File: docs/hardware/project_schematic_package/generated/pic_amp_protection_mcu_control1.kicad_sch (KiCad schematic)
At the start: 9 parts, among them J3 LCD_I2C, Q1 Q_NMOS, U1 PIC16F18855-xSO

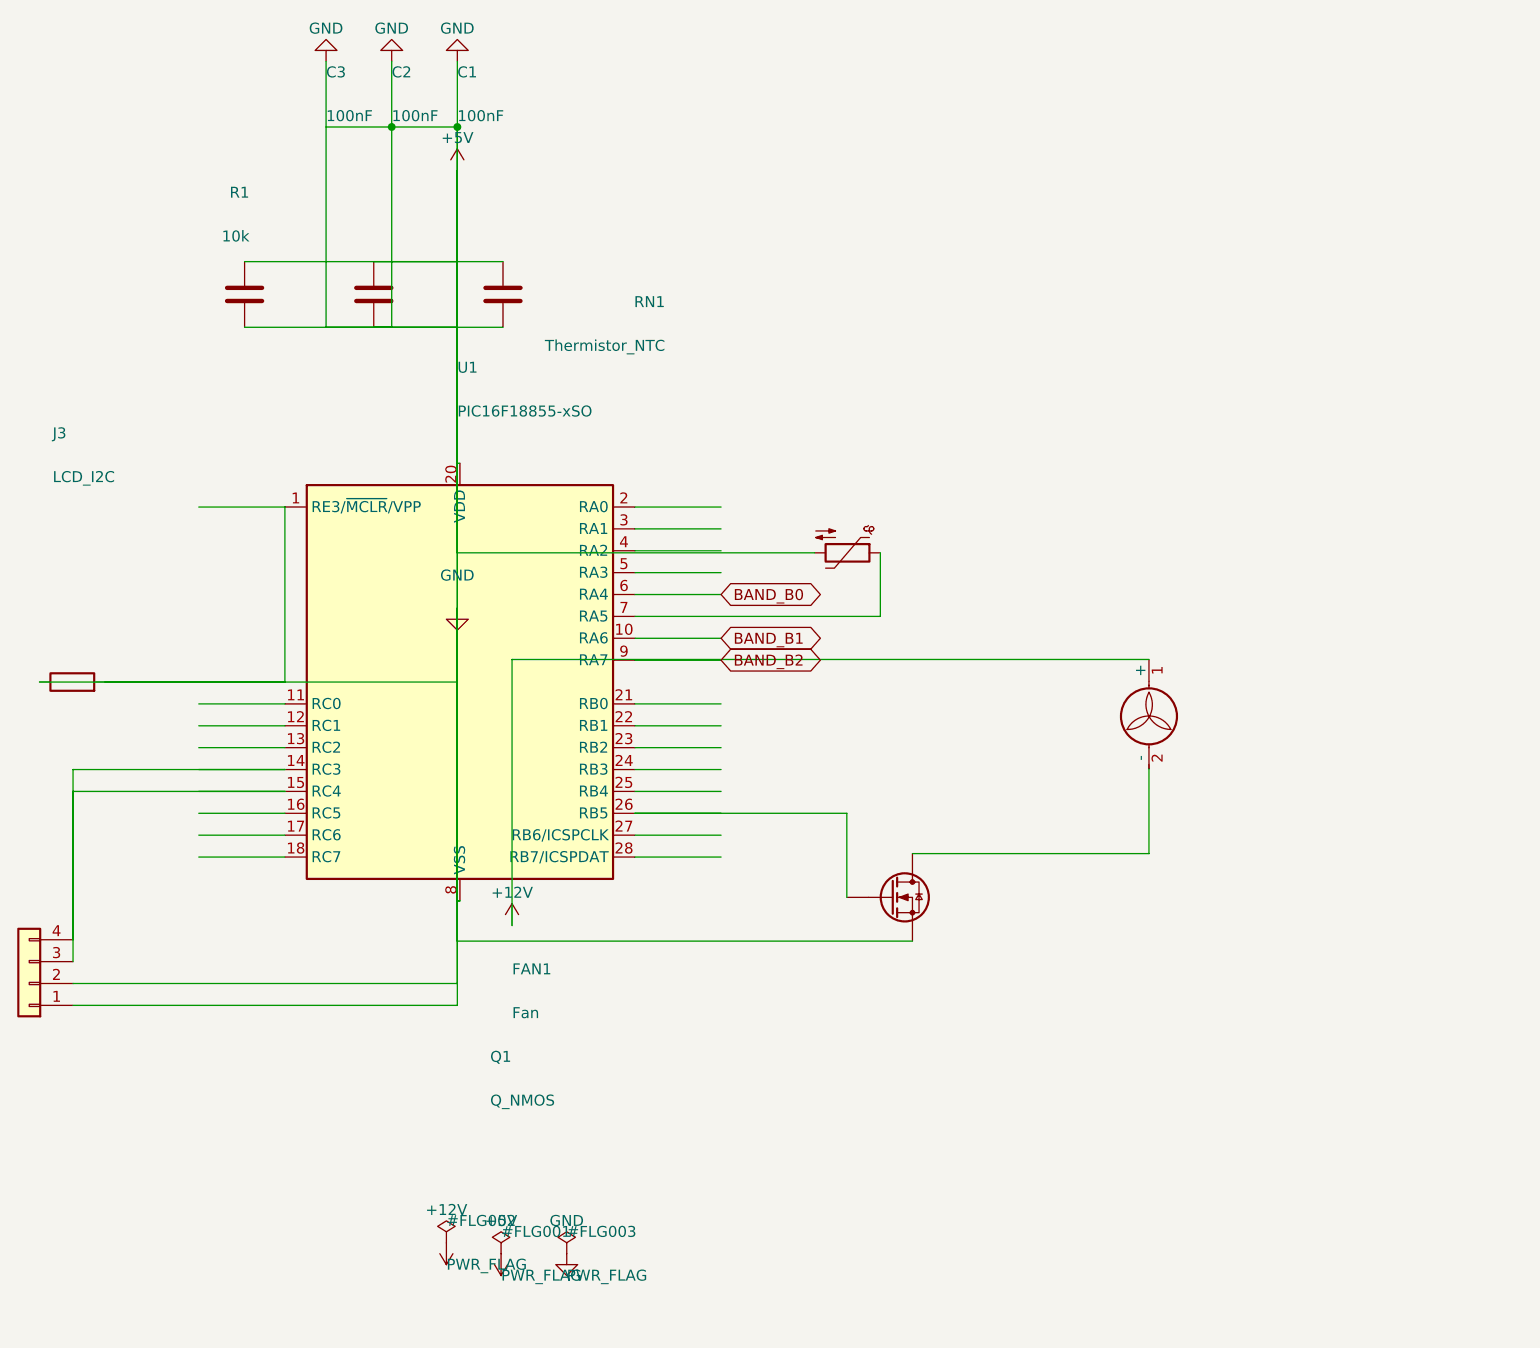
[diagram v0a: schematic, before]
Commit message: Add external interface connectors to complete MCU wiring
- J4 PTT_COMP_IF: PTT, comparator reset, overcurrent fault, GND
- J5 ENCODER: encoder A/B/switch, GND
- J6 TX_SEQ_TRIP: TX, TX_VCC, TX_BIAS, trip status, GND
- J7 SWR_SENSE: SWR1/SWR2 forward/reflected, GND
- J8 ANALOG_SENSE: current, overdrive, drain sense, GND

Wires every previously-unconnected U1 pin to one of these headers.
ERC unconnected-pin count: 17 -> 0. Remaining ERC output is limited to
pre-existing lib_symbol_mismatch/endpoint_off_grid warnings and the
standard PWR_FLAG-on-GND power_output/power_output pairing, consistent
with patterns already present in this file.
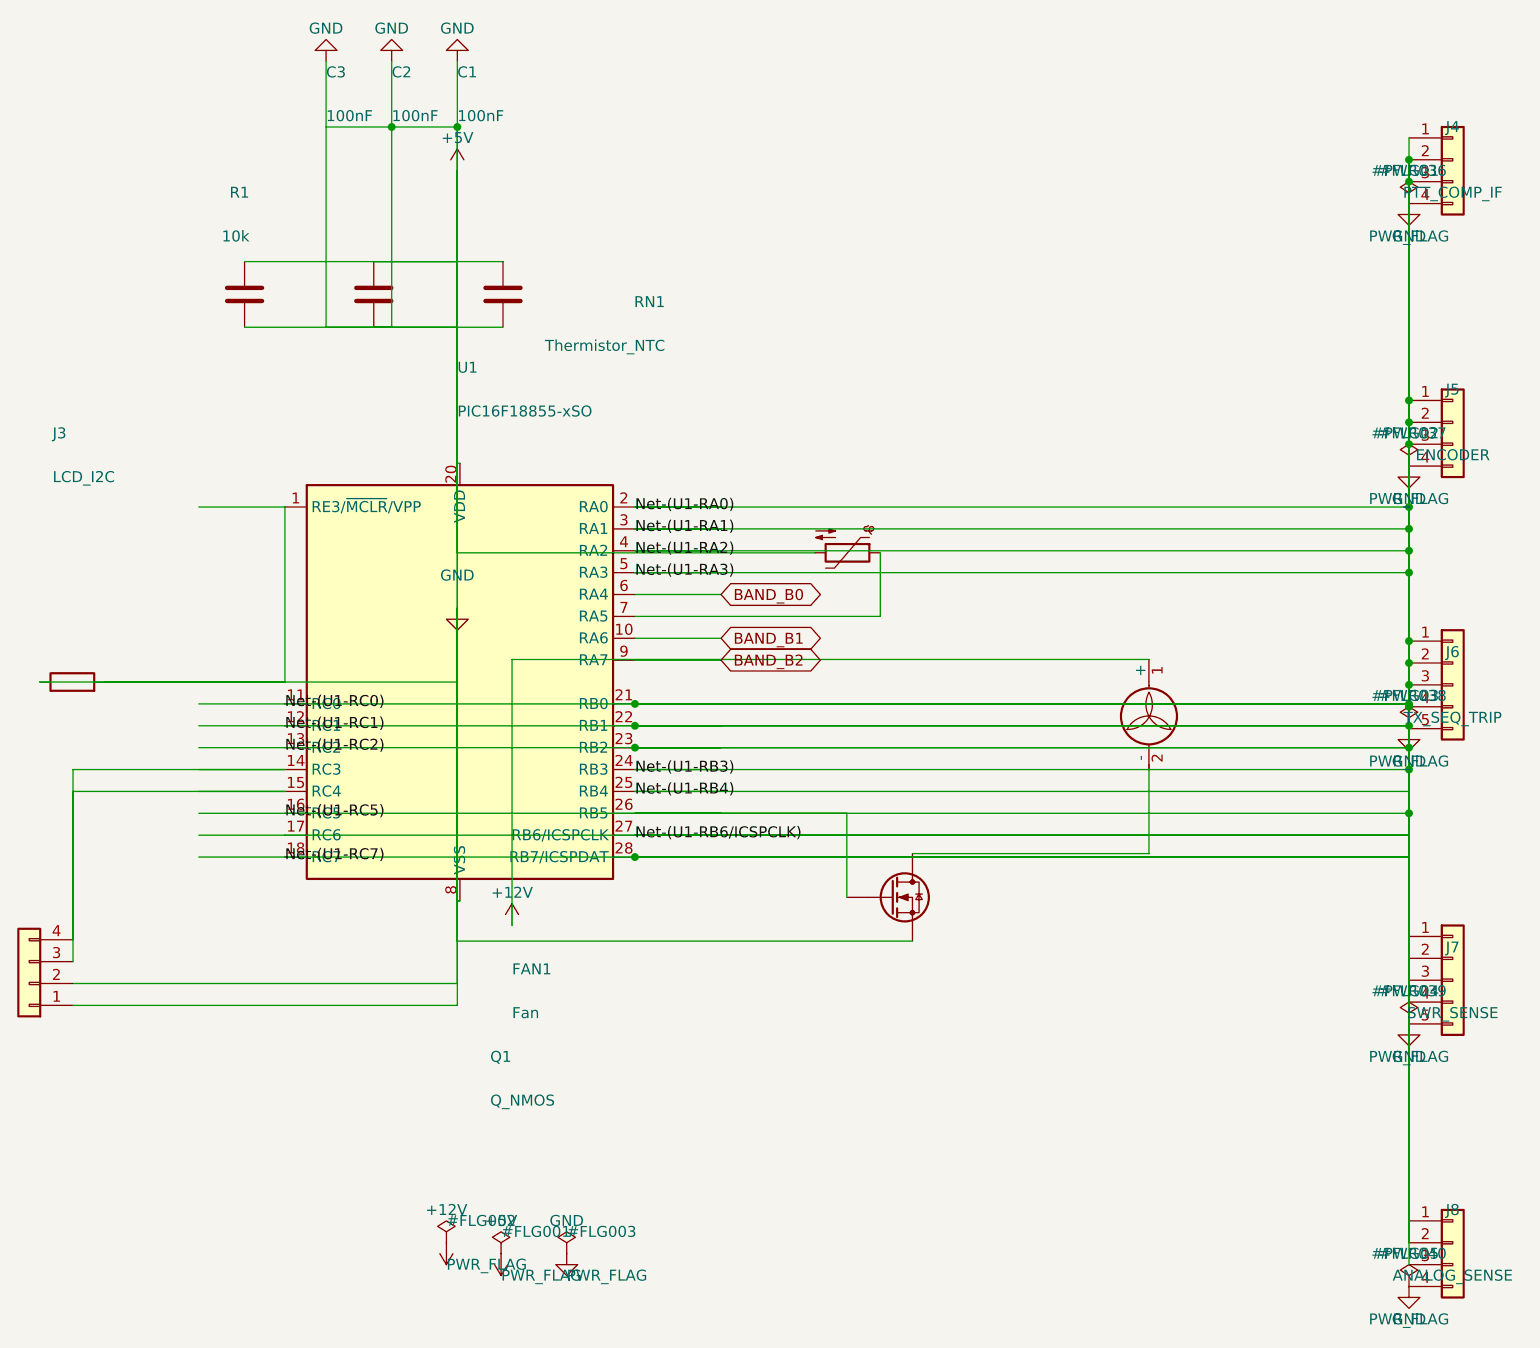
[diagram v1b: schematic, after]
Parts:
- added J4: PTT_COMP_IF, symbol Connector_Generic:Conn_01x04
- added J5: ENCODER, symbol Connector_Generic:Conn_01x04
- added J6: TX_SEQ_TRIP, symbol Connector_Generic:Conn_01x05
- added J7: SWR_SENSE, symbol Connector_Generic:Conn_01x05
- added J8: ANALOG_SENSE, symbol Connector_Generic:Conn_01x04
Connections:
- net +5V: now also J4.4 (Pin_4), J5.4 (Pin_4), J6.5 (Pin_5), J7.5 (Pin_5), J8.4 (Pin_4)
- net Net-(U1-RA0): now reaches U1.11 (RC0)
- net Net-(U1-RA0): now also Q1.G, U1.12 (RC1), U1.13 (RC2), U1.16 (RC5), U1.17 (RC6), U1.18 (RC7), U1.2 (RA0), U1.21 (RB0), U1.22 (RB1), U1.23 (RB2), U1.24 (RB3), U1.25 (RB4), U1.26 (RB5), U1.27 (RB6/ICSPCLK), U1.28 (RB7/ICSPDAT), U1.3 (RA1), U1.4 (RA2), U1.5 (RA3), J4.1 (Pin_1), J4.2 (Pin_2), J4.3 (Pin_3), J5.1 (Pin_1), J5.2 (Pin_2), J5.3 (Pin_3), J6.1 (Pin_1), J6.2 (Pin_2), J6.3 (Pin_3), J6.4 (Pin_4), J7.1 (Pin_1), J7.2 (Pin_2), J7.3 (Pin_3), J7.4 (Pin_4), J8.1 (Pin_1), J8.2 (Pin_2), J8.3 (Pin_3)
